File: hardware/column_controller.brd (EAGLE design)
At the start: 35.6 x 54.6 mm, 45 parts, among them J4 JTAG, U1 ESP-WROVER-32ESP-WROVER-32, U2 3.3V, U3 CP2102N

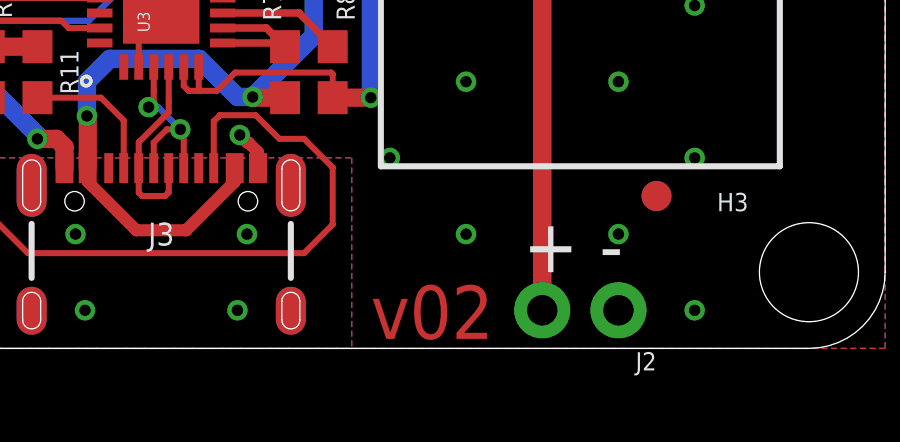
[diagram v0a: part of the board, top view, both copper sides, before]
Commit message: bump column controller to v03
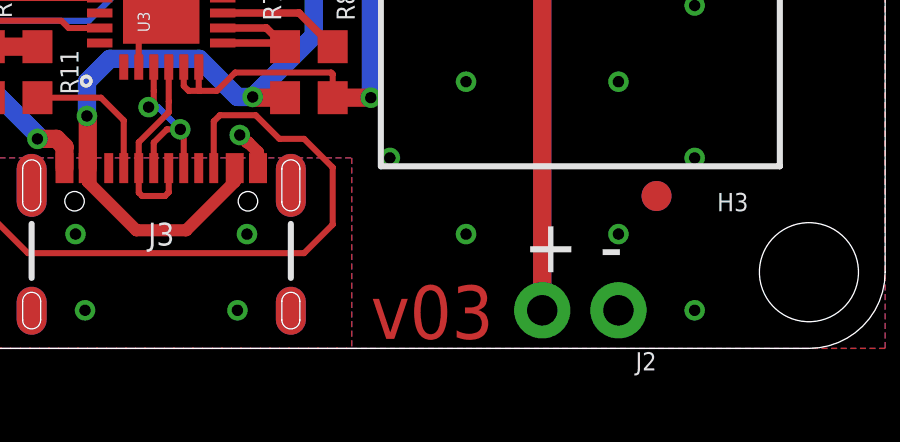
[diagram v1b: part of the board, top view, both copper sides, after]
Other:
- board text added: "v03"
- board text removed: "v02"
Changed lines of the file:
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@@
 <wire x1="33.02" y1="54.61" x2="2.54" y2="54.61" width="0" layer="20"/>
 <wire x1="2.54" y1="54.61" x2="0" y2="52.07" width="0" layer="20" curve="90"/>
-<text x="18.415" y="0.3175" size="1.778" layer="1" font="vector" ratio="15">v02</text>
+<text x="18.415" y="0.3175" size="1.778" layer="1" font="vector" ratio="15">v03</text>
 <text x="23.495" y="2.54" size="1.778" layer="21" font="vector" ratio="15">+</text>
 <text x="26.035" y="2.54" size="1.778" layer="21" font="vector" ratio="15">-</text>
@@
 <elements>
 <element name="FRAME1" library="SparkFun-Aesthetics" package="CREATIVE_COMMONS" value="FRAME-LEDGER" x="21.59" y="-8.89" smashed="yes">
-<attribute name="DESIGNER" value="" x="21.59" y="-8.89" size="1.778" layer="27" font="vector" ratio="15" display="off"/>
-<attribute name="REV" value="" x="21.59" y="-8.89" size="1.778" layer="27" font="vector" ratio="15" display="off"/>
+<attribute name="DESIGNER" value="Owen Lyke" x="21.59" y="-8.89" size="1.778" layer="27" font="vector" ratio="15" display="off"/>
+<attribute name="REV" value="v03" x="21.59" y="-8.89" size="1.778" layer="27" font="vector" ratio="15" display="off"/>
 </element>
 <element name="U1" library="SparkFun-RF" package="ESP-WROVER-32" value="ESP-WROVER-32ESP-WROVER-32" x="7.62" y="59.69" smashed="yes">
